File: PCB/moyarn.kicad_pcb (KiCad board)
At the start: 2 copper layers, 58 x 50 mm, 10 parts, among them U1 WeAct_Buck_DCDC, U2 WeAct_USBPD_to_DC, U3 TMC2209_SILENTSTEPSTICK

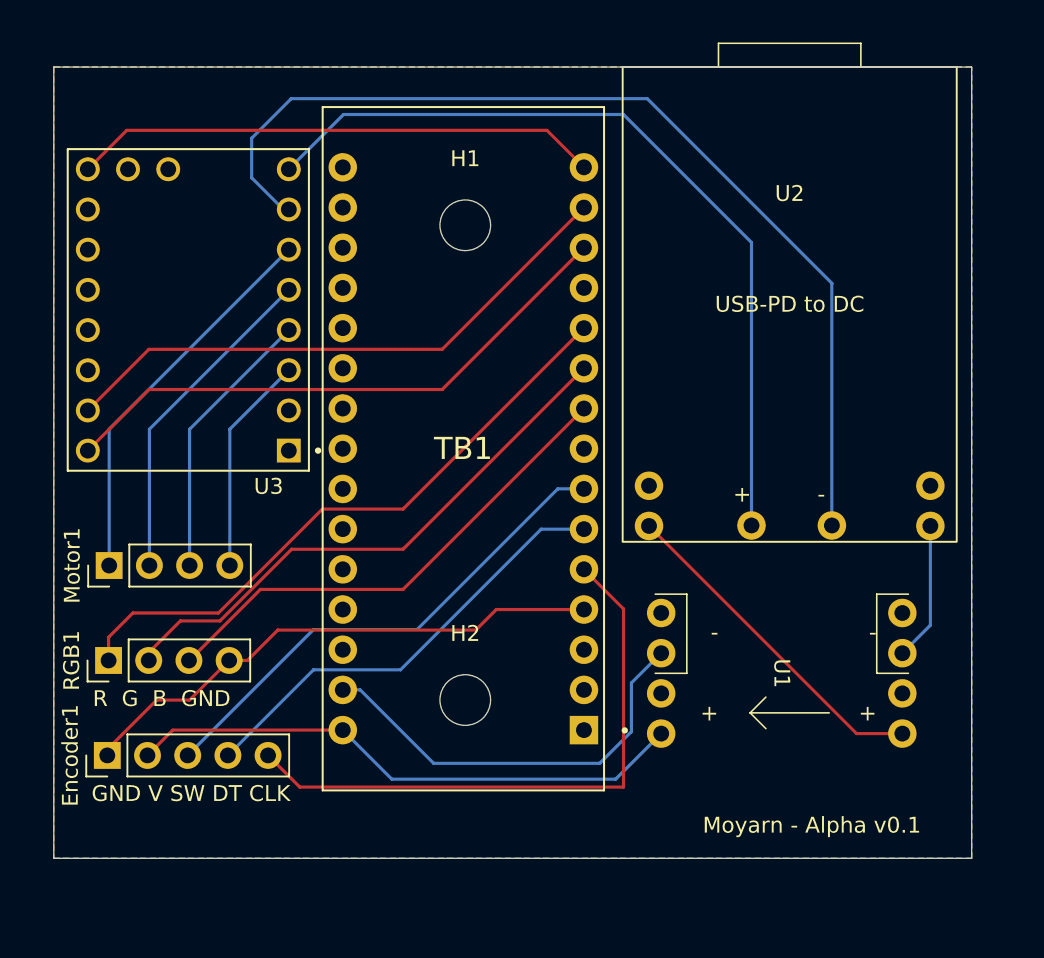
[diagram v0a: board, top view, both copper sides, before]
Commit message: change arduino-nano to rp2040-zero
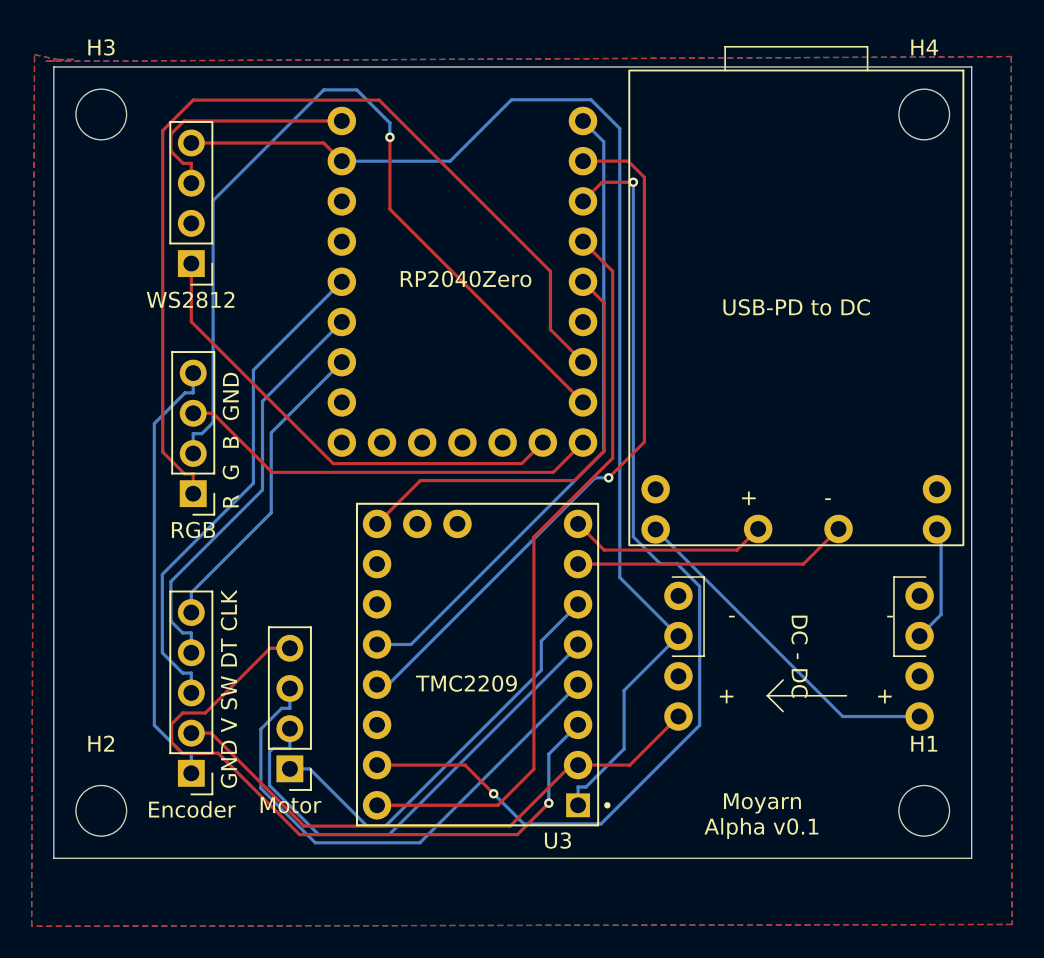
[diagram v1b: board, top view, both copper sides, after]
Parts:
- removed TB1: ARDUINO_NANO, footprints:ARDUINO_NANO_snapeda
- added H3: MountingHole, MountingHole:MountingHole_3.2mm_M3, F.Cu at (131.0, 64.0)
- added H4: MountingHole, MountingHole:MountingHole_3.2mm_M3, F.Cu at (183.0, 64.0)
- added U4: rp2040-zero, footprints:rp2040-zero-tht_kleeb, F.Cu at (153.8, 74.6)
- added WS2812: Conn_01x04_Pin, Connector_PinHeader_2.54mm:PinHeader_1x04_P2.54mm_Vertical, F.Cu at (136.7, 73.4)
- DC - DC: renamed from U1
- U3: value TMC2209_SILENTSTEPSTICK -> TMC2209
- moved H1 47.0 mm to (183.0, 108.0)
- moved U3 28.9 mm to (154.8, 98.8)
- moved H2 24.0 mm to (131.0, 108.0)
- moved Motor 17.2 mm to (142.9, 105.3), turned to 180 degrees
- moved RGB 11.8 mm to (136.8, 88.0), turned to 180 degrees
- moved Encoder 5.43 mm to (136.7, 105.6), turned to 180 degrees
- moved DC - DC 1.53 mm to (175.1, 98.2)
- moved U2 0.47 mm to (174.9, 76.2)
- renumbered Encoder1 to Encoder, Motor1 to Motor, RGB1 to RGB
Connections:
- U3 pad 1: unconnected-(U3-GND-Pad1) -> V5-
- U3 pad 12: unconnected-(U3-UART-Pad12) -> RX
- U3 pad 13: unconnected-(U3-SPRD-Pad13) -> TX
- U3 pad 2: unconnected-(U3-VIO-Pad2) -> V5+
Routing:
- net V5-: track 26.7 -> 77.1 mm
- net MD20-: track 63.5 -> 17.4 mm
- net RX: track 0.00 -> 44.3 mm, vias 0 -> 1
- net TX: track 0.00 -> 40.8 mm
- net MD20+: track 51.9 -> 12.6 mm
- net LED-DIN: track 0.00 -> 30.1 mm
- net MB2: track 13.9 -> 43.4 mm, vias 0 -> 1
- net STEP: track 36.7 -> 64.9 mm, vias 0 -> 2
- net LED-R: track 39.6 -> 60.4 mm
- net LED-G: track 35.4 -> 54.5 mm, vias 0 -> 1
- net EN-CLK: track 38.1 -> 19.8 mm
- net V5+: track 35.6 -> 51.2 mm
- net MB1: track 17.5 -> 33.0 mm
- net DIR: track 36.7 -> 47.0 mm
- net MA1: track 21.1 -> 30.5 mm
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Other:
- board text added: "Moyarn Alpha v0.1"
- board text added: "RP2040Zero"
- board text added: "TMC2209"
- board text added: "USB-PD to DC"
- board text removed: "Moyarn - Alpha v0.1"

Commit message: pcb error mod and source mod
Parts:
- DC to DC: renamed from DC - DC
- moved WS2812 9.96 mm to (141.4, 82.2)
- moved RGB 6.40 mm to (134.0, 82.2)
- moved Encoder 6.24 mm to (134.0, 100.0)
- moved Motor 5.43 mm to (142.0, 100.0)
- moved G*** 2.32 mm to (175.5, 76.8)
- moved H2 2.00 mm to (133.0, 108.0)
- moved H3 2.00 mm to (133.0, 64.0)
- moved DC to DC 1.77 mm to (175.1, 100.0)
- turned U3 to 0 degrees
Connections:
- Encoder pad 1: GND -> V5-
- RGB pad 4: GND -> V5-
- U4 pad 17: EN-CLK -> EN-SW
- U4 pad 19: EN-SW -> EN-CLK
- U4 pad 7: LED-R -> LED-B
- U4 pad 9: LED-B -> LED-R
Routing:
- net V5+: track 51.2 -> 92.3 mm
- net STEP: track 64.9 -> 24.8 mm, vias 2 -> 0
- net EN: track 27.5 -> 66.5 mm
- net MB2: track 43.4 -> 7.49 mm, vias 1 -> 0
- net LED-R: track 60.4 -> 30.1 mm
- net MD20-: track 17.4 -> 46.4 mm
- net GND: track 27.9 -> 0.00 mm
- net DIR: track 47.0 -> 19.4 mm
- net MD20+: track 12.6 -> 38.9 mm
- net MB1: track 33.0 -> 7.49 mm
- net MA1: track 30.5 -> 7.49 mm
- net LED-B: track 27.0 -> 47.4 mm
- net MA2: track 26.6 -> 7.49 mm
- net LED-G: track 54.5 -> 40.2 mm, vias 1 -> 0
- net V5-: track 77.1 -> 90.6 mm
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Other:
- board size 58 x 50 mm -> 56 x 50 mm
- board text added: "D-In V GND"
- board text added: "Moyarn Alpha v0.2"
- board text added: "PD to DC"
- board text removed: "Moyarn Alpha v0.1"
- board text removed: "USB-PD to DC"

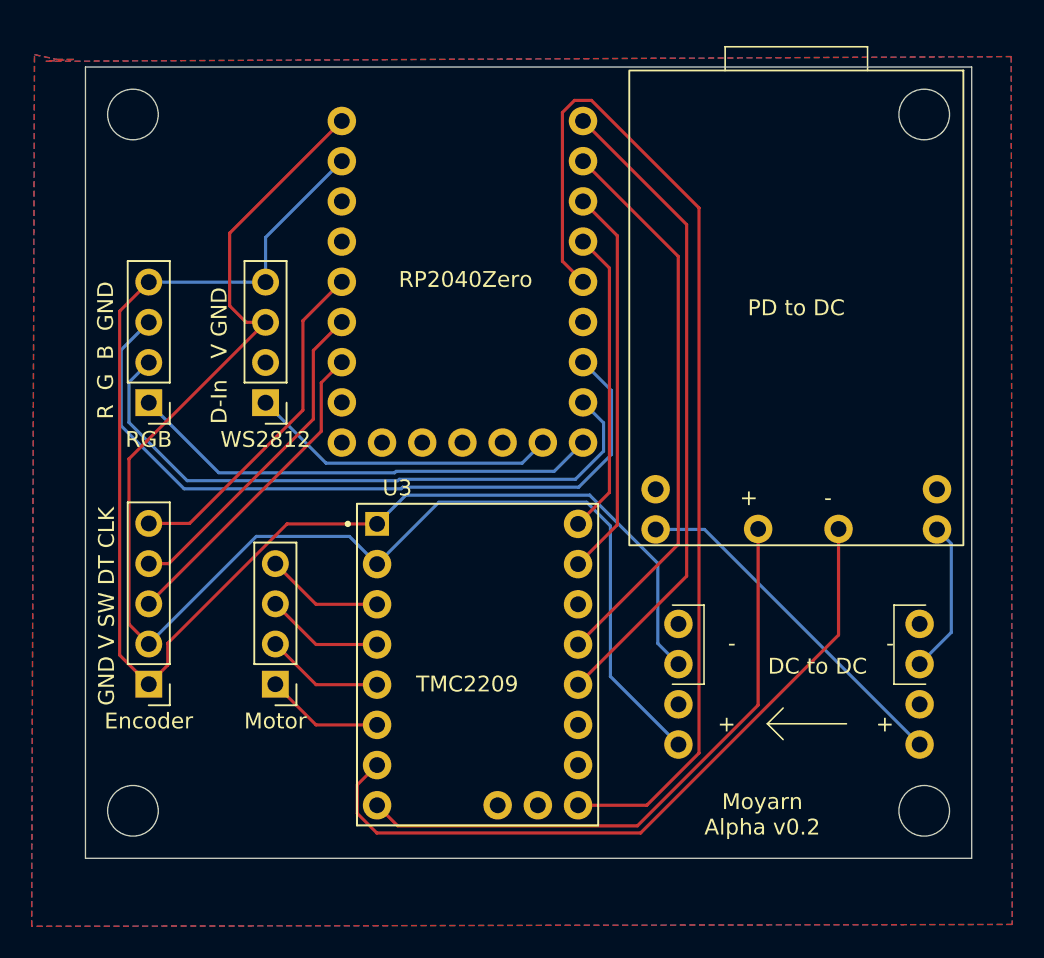
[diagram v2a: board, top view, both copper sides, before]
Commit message: via pad size change 1.8 to 1.7
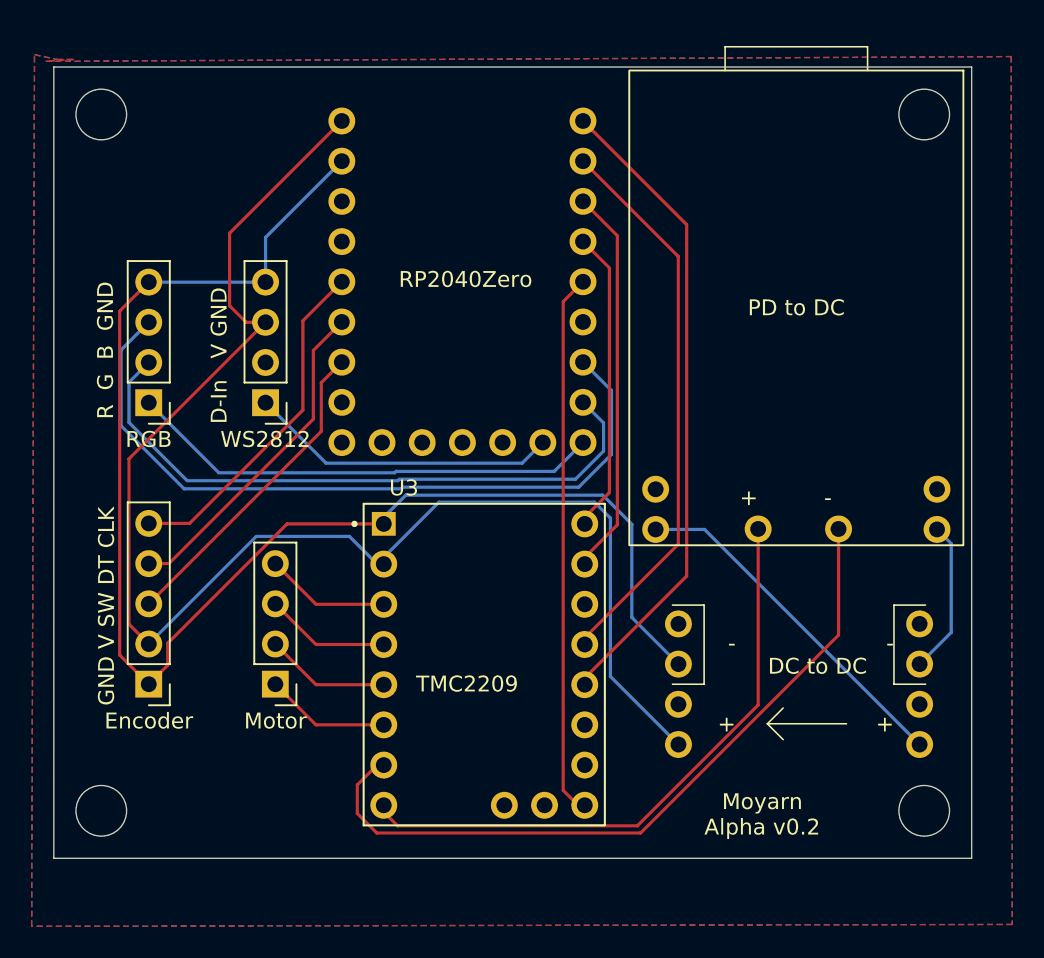
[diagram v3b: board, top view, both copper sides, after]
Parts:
- moved H2 2.00 mm to (131.0, 108.0)
- moved H3 2.00 mm to (131.0, 64.0)
- moved U3 0.42 mm to (155.2, 98.8)
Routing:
- net EN: track 66.5 -> 34.0 mm
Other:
- board size 56 x 50 mm -> 58 x 50 mm
